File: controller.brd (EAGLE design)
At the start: 100 x 80 mm, 29 parts, among them IC1 7805DT, J1 POWER_JACKSLT, J2 POWER_JACKSLT, Q1 MOSFET-NCHANNELBSS123LT1G, Q2 MOSFET-PCHANNEL, Q3 MOSFET-NCHANNELFDD8780, Q5 MMBT4403, U1 ATMEGA328P

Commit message: began layout of mcu section
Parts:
- removed BAT1: (no value), SparkFun-Electromechanical:BATTCON_12MM_PTH
- removed C3: (no value), adafruit:E22-10
- added U$2: DS1307SO8, SparkFun-FreqCtrl:SO08
- added Y1: 16MHz, SparkFun-FreqCtrl:RESONATOR-SMD
- added Y2: (no value), SparkFun-FreqCtrl:CRYSTAL-32KHZ-SMD
- moved U1 5.08 mm to (27.9, 44.5)
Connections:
- removed net +: BAT1.VCC@1
- removed net -: BAT1.GND
- removed net 3.3V: C3.-
- new net DTR: JP2.1
- new net N$1: U1.7, Y1.1
- new net N$4: Y1.3
- new net N$6: U$2.1, Y2.X2
- new net N$7: U$2.2, Y2.X1
- new net RXI: JP2.3
- new net TXO: JP2.2
- new net VCC: JP2.4
- net GND: now also C5.1, JP2.5, Y1.2
- net N$2: now also C5.2; no longer C3.+
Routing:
- net N$2: track 0.08 -> 26.7 mm
- net N$10: track 55.3 -> 76.0 mm
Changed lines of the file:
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@@
 <element name="C5" library="adafruit" package="C0805" value="" x="68.58" y="19.05" rot="R180"/>
 <element name="U$7" library="jt_parts" package="RESISTOR-0805" value="" x="44.45" y="20.32"/>
-<element name="BAT1" library="SparkFun-Electromechanical" package="BATTCON_12MM_PTH" value="" x="81.28" y="41.91"/>
-<element name="U1" library="SparkFun-DigitalIC" package="TQFP32-08" value="ATMEGA328P" x="33.02" y="44.45" rot="R45">
-<attribute name="PROD_ID" value="IC-09069" x="33.02" y="44.45" size="1.778" layer="27" rot="R45" display="off"/>
+<element name="U1" library="SparkFun-DigitalIC" package="TQFP32-08" value="ATMEGA328P" x="27.94" y="44.45" rot="R45">
+<attribute name="PROD_ID" value="IC-09069" x="27.94" y="44.45" size="1.778" layer="27" rot="R45" display="off"/>
 </element>
 <element name="S4" library="SparkFun-Electromechanical" package="TACTILE-PTH-SIDEEZ" value="SWITCH-MOMENTARY-2SIDE_EZ" x="76.2" y="57.15" rot="R180"/>
@@
 <element name="S2" library="SparkFun-Electromechanical" package="TACTILE-PTH-SIDEEZ" value="SWITCH-MOMENTARY-2SIDE_EZ" x="64.77" y="6.35"/>
 <element name="S3" library="SparkFun-Electromechanical" package="TACTILE-PTH-SIDEEZ" value="SWITCH-MOMENTARY-2SIDE_EZ" x="76.2" y="6.35"/>
-<element name="C3" library="adafruit" package="E22-10" value="" x="53.34" y="27.94" rot="R270"/>
+<element name="U$2" library="SparkFun-FreqCtrl" package="SO08" value="DS1307SO8" x="45.72" y="41.91"/>
+<element name="Y1" library="SparkFun-FreqCtrl" package="RESONATOR-SMD" value="16MHz" x="25.4" y="36.83">
+<attribute name="PROD_ID" value="XTAL-08900" x="25.4" y="36.83" size="1.778" layer="27" display="off"/>
+</element>
+<element name="Y2" library="SparkFun-FreqCtrl" package="CRYSTAL-32KHZ-SMD" value="" x="45.72" y="34.29" rot="R180"/>
 </elements>
 <signals>
@@
 <contactref element="Q5" pad="3"/>
 <contactref element="U$4" pad="2"/>
+<contactref element="C5" pad="1"/>
 <polygon width="0.254" layer="1" isolate="0.254" thermals="no">
 <vertex x="67.945" y="25.4"/>
@@
 <vertex x="88.9" y="11.43"/>
 <vertex x="86.36" y="8.89"/>
-<vertex x="86.36" y="6.35"/>
-<vertex x="12.7" y="6.35"/>
+<vertex x="86.36" y="0"/>
+<vertex x="12.7" y="0"/>
 <vertex x="12.7" y="8.89"/>
 <vertex x="10.16" y="11.43"/>
@@
 <wire x1="34.907284375" y1="26.017284375" x2="35.56" y2="26.67" width="1.524" layer="1"/>
 <via x="69.977" y="21.209" extent="1-16" drill="0.6096"/>
+<contactref element="Y1" pad="2"/>
+<contactref element="JP2" pad="5"/>
 <wire x1="69.977" y1="21.209" x2="70.89" y2="23.12" width="0" layer="19" extent="1-1"/>
+<wire x1="69.43" y1="19.05" x2="69.977" y2="21.209" width="0" layer="19" extent="1-1"/>
+<wire x1="68.58" y1="17.907" x2="69.43" y2="19.05" width="0" layer="19" extent="1-1"/>
+<wire x1="69.58" y1="16.51" x2="68.58" y2="17.907" width="0" layer="19" extent="1-1"/>
+<wire x1="71.882" y1="16.764" x2="69.58" y2="16.51" width="0" layer="19" extent="1-1"/>
 <wire x1="68.41" y1="24.13" x2="70.89" y2="23.12" width="0" layer="19" extent="1-1"/>
 <wire x1="72.81" y1="20.32" x2="69.977" y2="21.209" width="0" layer="19" extent="1-1"/>
-<wire x1="68.58" y1="17.907" x2="69.977" y2="21.209" width="0" layer="19" extent="1-1"/>
-<wire x1="69.58" y1="16.51" x2="68.58" y2="17.907" width="0" layer="19" extent="1-1"/>
-<wire x1="71.882" y1="16.764" x2="69.58" y2="16.51" width="0" layer="19" extent="1-1"/>
 <wire x1="40.64" y1="21.17" x2="64.6" y2="18.73" width="0" layer="19" extent="1-1"/>
 <wire x1="36.83" y1="29.21" x2="38.227" y2="27.813" width="0" layer="19" extent="1-1"/>
@@
 <wire x1="14.61" y1="16.55" x2="30.48" y2="21.17" width="0" layer="19" extent="1-1"/>
 <wire x1="17.78" y1="8.89" x2="14.61" y2="16.55" width="0" layer="19" extent="1-1"/>
+<wire x1="8.89" y1="46.99" x2="32.893" y2="27.813" width="0" layer="19" extent="1-1"/>
+<wire x1="25.4" y1="36.83" x2="17.78" y2="8.89" width="0" layer="19" extent="1-1"/>
 </signal>
 <signal name="RCK">
@@
 <contactref element="Q1" pad="3"/>
 <contactref element="Q2" pad="1"/>
-<wire x1="59.69" y1="21.082" x2="59.69" y2="19.05" width="0" layer="19" extent="1-16"/>
-<wire x1="59.69" y1="19.05" x2="60.96" y2="17.78" width="0" layer="19" extent="1-16"/>
-<wire x1="60.96" y1="17.78" x2="62.4" y2="17.78" width="0.254" layer="1"/>
 <wire x1="25.273" y1="30.48" x2="25.273" y2="31.115" width="0.254" layer="1"/>
 <wire x1="25.273" y1="30.48" x2="27.67" y2="30.48" width="0.254" layer="1"/>
@@
 <wire x1="39.37" y1="31.75" x2="40.64" y2="30.48" width="0.254" layer="1"/>
 <wire x1="40.64" y1="30.48" x2="40.64" y2="25.4" width="0.254" layer="1"/>
-<wire x1="40.64" y1="25.4" x2="43.18" y2="22.86" width="0.254" layer="1"/>
-<wire x1="43.18" y1="22.86" x2="57.912" y2="22.86" width="0" layer="19" extent="1-16"/>
-<wire x1="57.912" y1="22.86" x2="59.69" y2="21.082" width="0" layer="19" extent="1-16"/>
+<wire x1="40.64" y1="25.4" x2="44.45" y2="21.59" width="0.254" layer="1"/>
 <wire x1="34.33" y1="7.62" x2="33.02" y2="7.62" width="0.254" layer="1"/>
 <wire x1="26.162" y1="26.924" x2="27.686" y2="26.924" width="0.254" layer="1"/>
@@
 <wire x1="32.385" y1="31.75" x2="31.115" y2="30.48" width="0.254" layer="1"/>
 <wire x1="27.686" y1="30.48" x2="27.67" y2="30.48" width="0.254" layer="1"/>
+<wire x1="44.45" y1="21.59" x2="44.45" y2="20.28" width="0.254" layer="1"/>
+<wire x1="44.45" y1="20.28" x2="46.95" y2="17.78" width="0.254" layer="1"/>
+<wire x1="46.95" y1="17.78" x2="62.4" y2="17.78" width="0.254" layer="1"/>
 </signal>
 <signal name="PWR-CNTRL">
@@
 <signal name="N$2">
 <contactref element="Q4" pad="3"/>
+<contactref element="C5" pad="2"/>
 <contactref element="U$7" pad="2"/>
+<wire x1="61.976" y1="20.32" x2="45.45" y2="20.32" width="0.254" layer="1"/>
+<wire x1="61.976" y1="24.13" x2="61.976" y2="20.32" width="0.254" layer="1"/>
 <wire x1="61.976" y1="24.13" x2="62.06" y2="24.13" width="0.254" layer="1"/>
-<contactref element="C3" pad="+"/>
-<wire x1="61.976" y1="24.13" x2="53.34" y2="39.37" width="0" layer="19" extent="1-1"/>
-<wire x1="45.45" y1="20.32" x2="61.976" y2="24.13" width="0" layer="19" extent="1-1"/>
+<wire x1="66.548" y1="19.05" x2="67.691" y2="19.05" width="0.254" layer="1"/>
+<wire x1="65.278" y1="20.32" x2="66.548" y2="19.05" width="0.254" layer="1"/>
+<wire x1="61.976" y1="20.32" x2="65.278" y2="20.32" width="0.254" layer="1"/>
+<wire x1="67.691" y1="19.05" x2="67.73" y2="19.05" width="0.254" layer="1"/>
 </signal>
 <signal name="PWM">
@@
 <vertex x="20.955" y="19.05"/>
 </polygon>
-</signal>
-<signal name="-">
-<contactref element="BAT1" pad="GND"/>
-</signal>
-<signal name="+">
-<contactref element="BAT1" pad="VCC@1"/>
 </signal>
 <signal name="12V-IN" class="1">
@@
 <wire x1="82.042" y1="21.59" x2="83.18" y2="21.55" width="2.032" layer="1"/>
 </signal>
-<signal name="3.3V">
-<contactref element="C3" pad="-"/>
+<signal name="N$1">
+<contactref element="U1" pad="7"/>
+<contactref element="Y1" pad="1"/>
+<wire x1="24.2" y1="36.83" x2="26.318884375" y2="40.000459375" width="0" layer="19" extent="1-1"/>
+</signal>
+<signal name="N$4">
+<contactref element="Y1" pad="3"/>
+</signal>
+<signal name="VCC">
+<contactref element="JP2" pad="4"/>
+</signal>
+<signal name="RXI">
+<contactref element="JP2" pad="3"/>
+</signal>
+<signal name="TXO">
+<contactref element="JP2" pad="2"/>
+</signal>
+<signal name="DTR">
+<contactref element="JP2" pad="1"/>
+</signal>
+<signal name="N$6">
+<contactref element="U$2" pad="1"/>
+<contactref element="Y2" pad="X2"/>
+<wire x1="44.45" y1="34.29" x2="43.815" y2="39.2938" width="0" layer="19" extent="1-1"/>
+</signal>
+<signal name="N$7">
+<contactref element="U$2" pad="2"/>
+<contactref element="Y2" pad="X1"/>
+<wire x1="46.99" y1="34.29" x2="45.085" y2="39.2938" width="0" layer="19" extent="1-1"/>
 </signal>
 </signals>

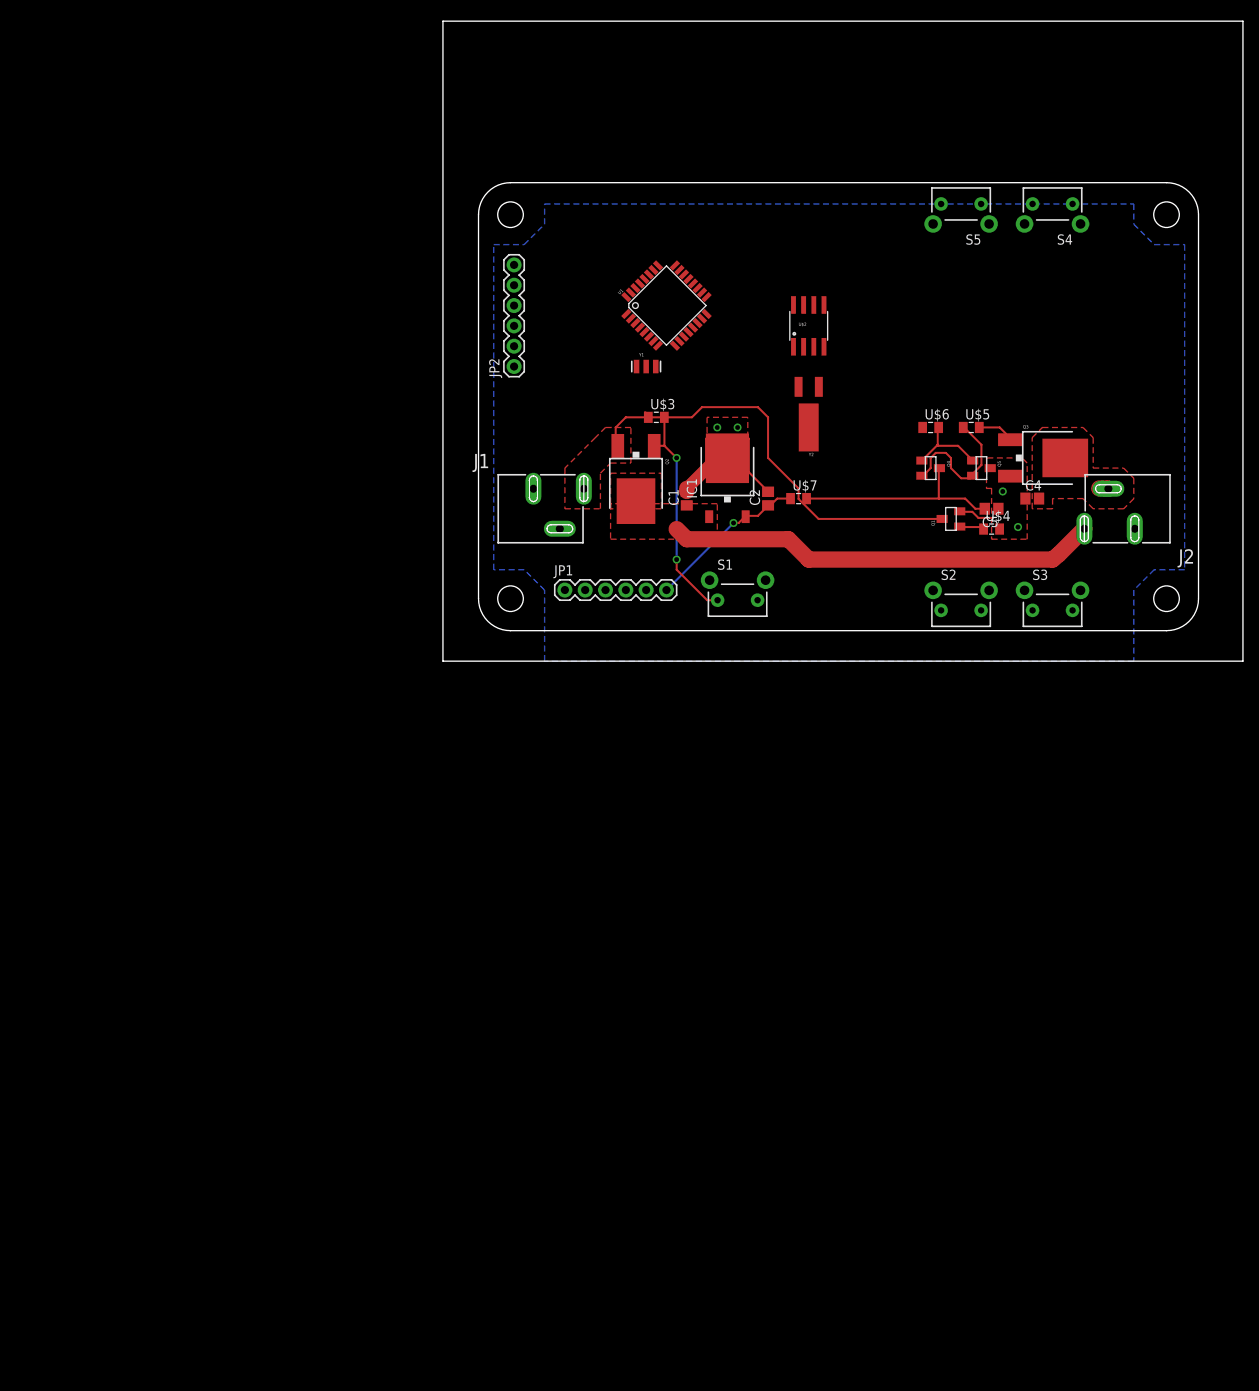
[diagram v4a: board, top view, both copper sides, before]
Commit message: completed micro section schematic. split power from led strip pwm sections.
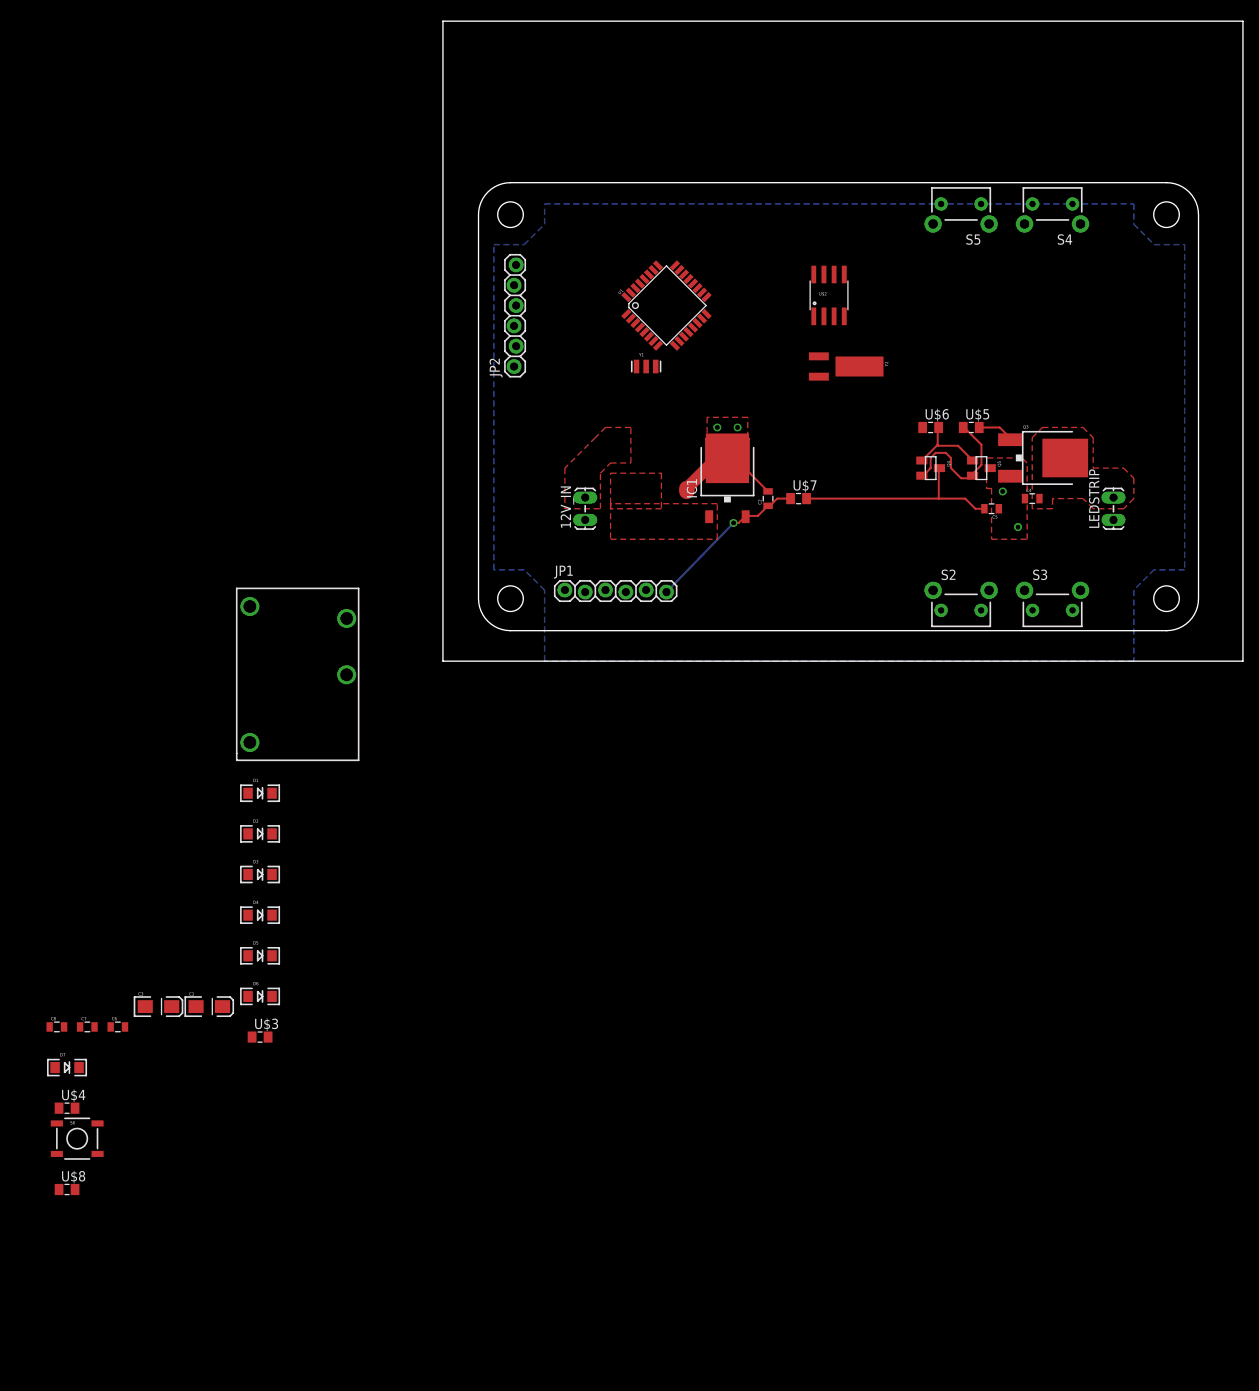
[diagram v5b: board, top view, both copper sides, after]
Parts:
- removed J1, J2: POWER_JACKSLT, SparkFun-Connectors:POWER_JACK_SLOT
- removed Q1: MOSFET-NCHANNELBSS123LT1G, SparkFun-DiscreteSemi:SOT23
- removed Q2: MOSFET-PCHANNEL, SparkFun-DiscreteSemi:DPAK
- added 12V_IN, LEDSTRIP: M02LOCK_LONGPADS, SparkFun-Connectors:1X02_LOCK_LONGPADS
- added C3: (no value), SparkFun-Capacitors:EIA3216-KIT
- added C6, C7, C8: (no value), SparkFun-Capacitors:0805
- added D1, D2, D3, D4, D5, D6: WHITE, SparkFun-LED:LED-1206
- added D7: GREEN, SparkFun-LED:LED-1206
- added S6: (no value), SparkFun-Electromechanical:TACTILE_SWITCH_SMD
- added U$8: (no value), jt_parts:RESISTOR-0805
- C1: device adafruit:C0805 -> SparkFun-Capacitors:EIA3216-KIT
- C2, C4, C5: device adafruit:C0805 -> SparkFun-Capacitors:0805
- JP1, JP2: device SparkFun-Connectors:1X06 -> SparkFun-Connectors:1X06_LOCK
- S1: value SWITCH-MOMENTARY-2SIDE_EZ -> (none); device SparkFun-Electromechanical:TACTILE-PTH-SIDEEZ -> SparkFun-Electromechanical:R_SW_TH
- U$3, U$4: value 10k -> (none)
- moved U$4 136.4 mm to (-47.0, -55.9)
- moved U$3 92.0 mm to (-22.9, -47.0)
- moved C1 87.2 mm to (-29.2, -43.2), turned to 0 degrees
- moved S1 63.5 mm to (-24.1, -10.2)
- moved U$2 4.58 mm to (48.3, 45.7)
- moved Y2 2.84 mm to (47.0, 36.8), turned to 270 degrees
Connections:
- removed net 12V-IN: J1.PWR, Q2.3, U$3.1
- removed net PWR-CNTRL: Q1.1, U$4.1
- new net N$11: C7.1, U1.20
- new net N$15: C8.2, S6.3, S6.4, U$8.2, U1.29
- new net N$8: 12V_IN.2, S1.P$2
- new net N$9: D1.A, D2.A, D3.A, D4.A, D5.A, D6.A, U$3.2
- new net NIGHT: U$3.1
- net 12V: now also C1.A, LEDSTRIP.1, S1.P$1, S1.P$3; no longer C1.1, J2.PWR, Q2.4
- net 12V-RETURN: now also LEDSTRIP.2; no longer J2.GND@2
- net 5V: now also C3.A, C6.1, U$4.2, U$8.1, U1.18, U1.4, U1.6
- net DTR: now also C8.1
- net GND: now also 12V_IN.1, C1.C, C3.C, C6.2, C7.2, D7.C, JP2.6, S6.1, S6.2, U1.21, U1.3, U1.5; no longer C1.2, J1.GND@2, Q1.2, S1.2, U$4.2
- net N$10: now also D7.A, U$4.1; no longer Q1.3, Q2.1, S1.1, U$3.2
- net N$4: now also U1.8
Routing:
- net N$10: track 76.0 -> 0.00 mm, vias 2 -> 0
- net 12V: track 54.1 -> 0.00 mm
- net 12V-IN: track 7.02 -> 0.00 mm
- net GND: track 31.1 -> 26.7 mm
- net PWR-CNTRL: track 3.27 -> 0.00 mm
- net 12V-RETURN: track 2.55 -> 1.28 mm
